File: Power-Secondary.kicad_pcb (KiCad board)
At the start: 2 copper layers, 82 x 66 mm, 37 parts, among them J1 SUPP PWR MON, J2 SUPP PWR 1, J3 SUPP PWR 2, J4 DCDC SUPPLY, J5 FUSE OUT, J6 SUPP OUT, J7 LV ENABLE, Q1 S1G1D2S2G2D1, Q1A1 IRFU5305PbF, Q1A2 IRFU5305PbF, Q1A3 IRFU5305PbF, Q1A4 IRFU5305PbF, Q2 S1G1D2S2G2D1, Q3 FDD86250-F085

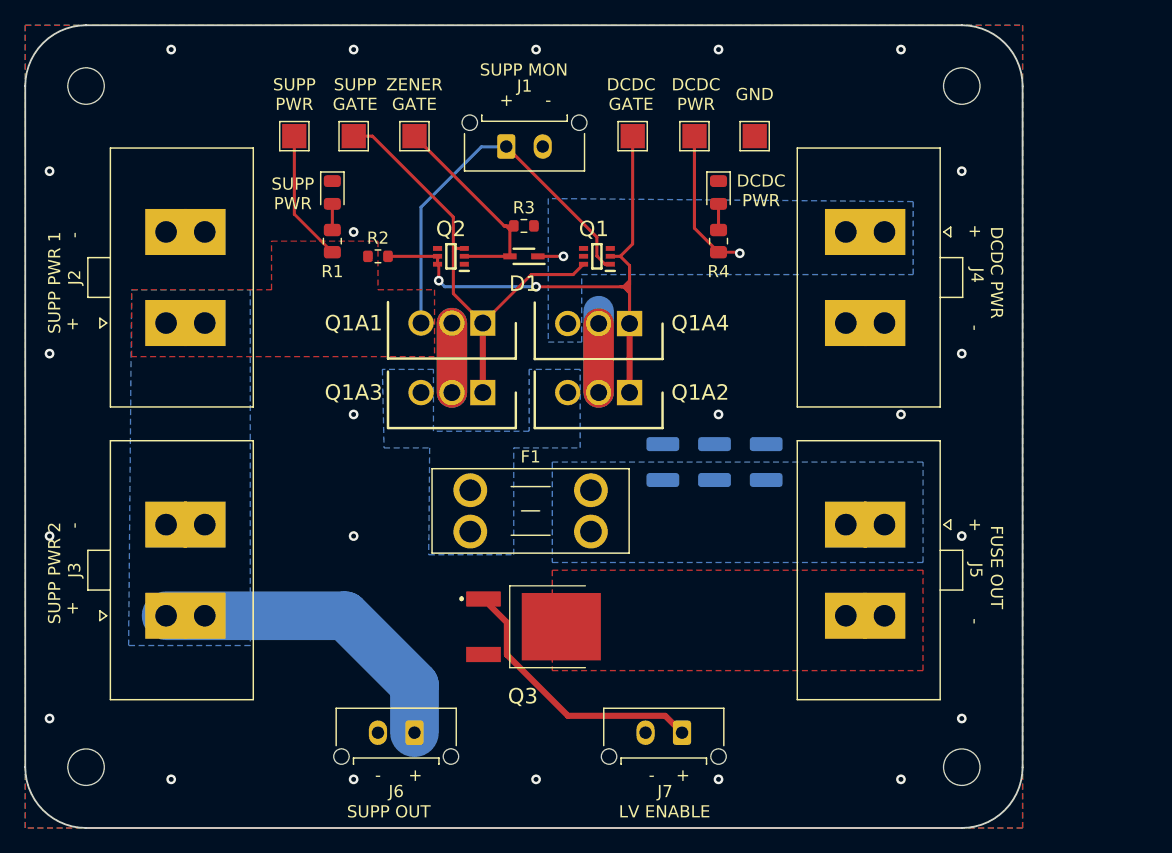
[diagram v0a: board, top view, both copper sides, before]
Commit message: Ltc4421 v1.0 (#12)
* LTC4421 Symbol creation

* early sch

* early sch

* changes

* Improved organization of sch

* added circuitry for sch

* Added MOSFET to symbol library

* Finished sch

* footprint assignments

* changes to Power Board sch

* CAD models, symbols update, and footprints

* Pull up and Pull down configs for VALID, DISABLE, SHDN, RETRY

* small changes

* Library fixes and sch changes

* Sch changes

* changes to sch

* assigned footprints

* Excel calculator

* Adjusted resistor divider values and specified more components in the BOM

* Completed BOM for the most part

* sch iteration 1 complete plssssssssss

* final footprint assignments

* initial layout

* added another current sense resistor

* fixed connector pinout

* change SHDN logic

* fixes to sch

* layout complete

* Layout fixes

* made all planes solid filled

* added supp mon connection

* constraint fixes

---------

Co-authored-by: choafe <cryn.hoang@gmail.com>
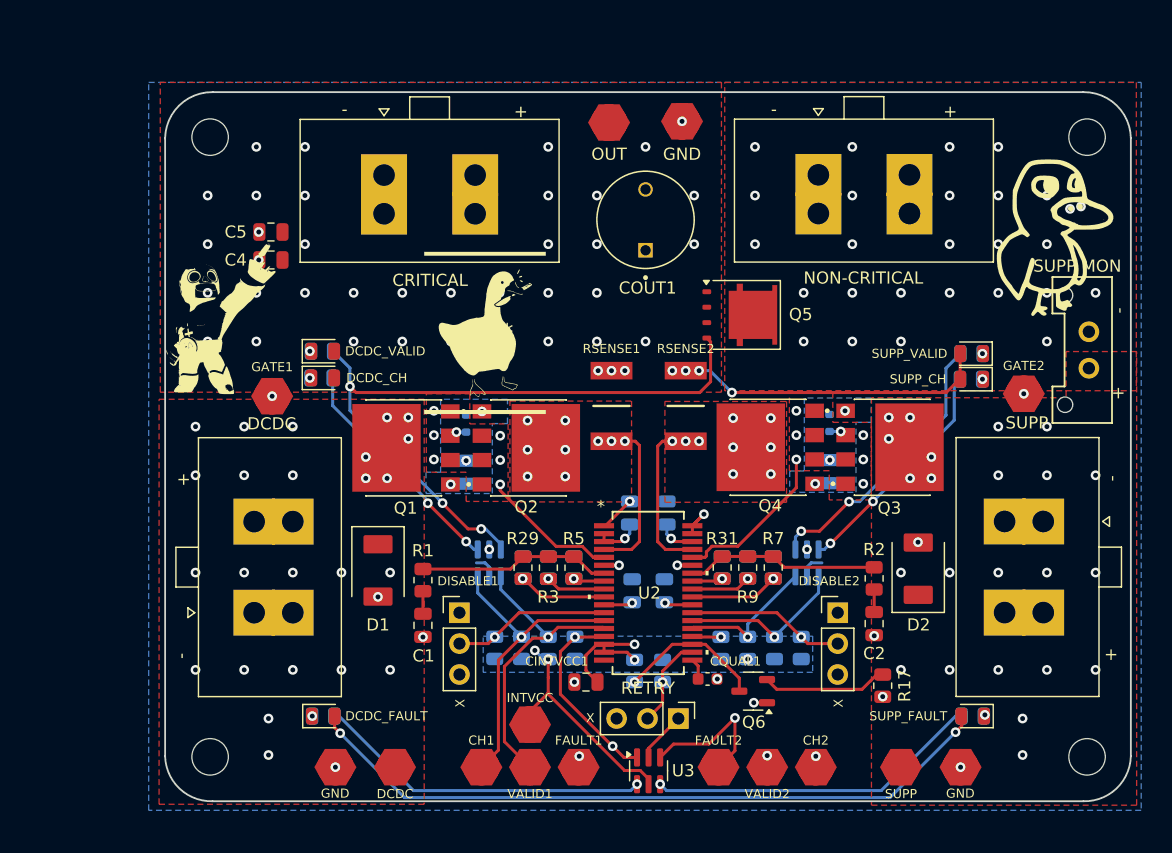
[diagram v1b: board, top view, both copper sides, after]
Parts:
- removed DS1: SUPP_PWR, Diode_SMD:D_0805_2012Metric
- removed DS2: DCDC_PWR, Diode_SMD:D_0805_2012Metric
- removed F1: Fuse, Fuse:Fuseholder_Blade_Mini_Keystone_3568
- removed J1: SUPP PWR MON, Connector_Molex:Molex_Micro-Fit_3.0_43650-0215_1x02_P3.00mm_Vertical
- removed J2: SUPP PWR 1, Connector_Molex:Molex_Sabre_43160-0102_1x02_P7.49mm_Vertical
- removed J3: SUPP PWR 2, Connector_Molex:Molex_Sabre_43160-0102_1x02_P7.49mm_Vertical
- removed J4: DCDC SUPPLY, Connector_Molex:Molex_Sabre_43160-0102_1x02_P7.49mm_Vertical
- removed J5: FUSE OUT, Connector_Molex:Molex_Sabre_43160-0102_1x02_P7.49mm_Vertical
- removed J6: SUPP OUT, Connector_Molex:Molex_Micro-Fit_3.0_43650-0215_1x02_P3.00mm_Vertical
- removed J7: LV ENABLE, Connector_Molex:Molex_Micro-Fit_3.0_43650-0215_1x02_P3.00mm_Vertical
- removed LOGO1: Dr Hallock, UTSVT_Special:Hallock_Image_Tiny
- removed LOGO2: UTSVT, UTSVT_Special:UTSVT_Logo_Symbol
- removed Q1A1, Q1A2, Q1A3, Q1A4: IRFU5305PbF, UTSVT_PowerSupp:SUP90P06-PCHAN-ENH-PWR-MOSFET
- removed TP1: SUPP_PWR, TestPoint:TestPoint_Pad_2.0x2.0mm
- removed TP2: DCDC_PWR, TestPoint:TestPoint_Pad_2.0x2.0mm
- removed TP3: ZENER_GATE, TestPoint:TestPoint_Pad_2.0x2.0mm
- removed TP4: DCDC_Gate, TestPoint:TestPoint_Pad_2.0x2.0mm
- removed TP5: Supp_Gate, TestPoint:TestPoint_Pad_2.0x2.0mm
- removed TP6: GND, TestPoint:TestPoint_Pad_2.0x2.0mm
- added ?: , , F.Cu at (113.5, 104.0)
- added ?: , , F.Cu at (164.9, 104.0)
- added C4: 10u, Capacitor_SMD:C_0805_2012Metric, F.Cu at (108.2, 62.3)
- added C5: 0.1u, Capacitor_SMD:C_0805_2012Metric, F.Cu at (108.2, 60.0)
- added CCPO1: 1u, Capacitor_SMD:C_0805_2012Metric, B.Cu at (137.7, 83.1)
- added CH1: TestPoint, UTSVT_Special:TestPoint_HEX_3mmID, F.Cu at (125.5, 104.0)
- added CH2: TestPoint, UTSVT_Special:TestPoint_HEX_3mmID, F.Cu at (153.0, 104.0)
- added CINTVCC1: 1u, Capacitor_SMD:C_0805_2012Metric, F.Cu at (134.1, 97.0)
- added CMOSFET1: 10u, Capacitor_SMD:C_0805_2012Metric, B.Cu at (124.2, 79.8)
- added CMOSFET3: 10u, Capacitor_SMD:C_0805_2012Metric, B.Cu at (154.2, 79.7)
- added COUT1: 1.2m, PowerBoardLib:EEUFS1C122LB, F.Cu at (139.0, 59.0)
- added CQUAL1: 500p, Capacitor_SMD:C_0603_1608Metric, F.Cu at (144.1, 96.8)
- added CRITICAL: PowerConn, Connector_Molex:Molex_Sabre_43160-0102_1x02_P7.49mm_Vertical, F.Cu at (117.5, 58.5)
- added CTMR1: 10u, Capacitor_SMD:C_0805_2012Metric, B.Cu at (137.9, 89.5)
- added CTMR2: 10u, Capacitor_SMD:C_0805_2012Metric, B.Cu at (140.6, 89.5)
- added D11: D_Zener, Diode_SMD:D_SOD-523, B.Cu at (154.1, 75.7)
- added D2: SMBJ15D-M3I, PowerBoardLib:P26_DO-214AA_SMB, F.Cu at (161.4, 89.8)
- added D9: D_Zener, Diode_SMD:D_SOD-523, B.Cu at (124.2, 75.8)
- added DCDC: TestPoint, UTSVT_Special:TestPoint_HEX_3mmID, F.Cu at (118.4, 104.0)
- added DCDC: PowerConn, Connector_Molex:Molex_Sabre_43160-0102_1x02_P7.49mm_Vertical, F.Cu at (110.0, 91.3)
- added DCDC_CH: LED, LED_SMD:LED_0805_2012Metric, F.Cu at (112.5, 72.0)
- added DCDC_FAULT: LED, LED_SMD:LED_0805_2012Metric, F.Cu at (112.5, 99.8)
- added DCDC_VALID: LED, LED_SMD:LED_0805_2012Metric, F.Cu at (112.5, 69.8)
- added DISABLE1: DIS1 Jumper, Connector_PinHeader_2.54mm:PinHeader_1x03_P2.54mm_Vertical, F.Cu at (123.7, 91.3)
- added DISABLE2: DIS2 Jumper, Connector_PinHeader_2.54mm:PinHeader_1x03_P2.54mm_Vertical, F.Cu at (154.8, 91.3)
- added FAULT1: TestPoint, UTSVT_Special:TestPoint_HEX_3mmID, F.Cu at (133.5, 104.0)
- added FAULT2: TestPoint, UTSVT_Special:TestPoint_HEX_3mmID, F.Cu at (145.0, 104.0)
- added G***: LOGO, LOGO, F.Cu at (103.8, 67.1)
- added G***: LOGO, LOGO, F.Cu at (125.8, 68.3)
- added G***: LOGO, LOGO, F.Cu at (172.6, 60.5)
- added G***: LOGO, LOGO, B.Cu at (112.8, 65.8)
- added G***: LOGO, LOGO, B.Cu at (166.2, 63.9)
- added G***: LOGO, LOGO, B.Cu at (139.1, 62.9)
- added GATE1: TestPoint, UTSVT_Special:TestPoint_HEX_3mmID, F.Cu at (108.3, 73.5)
- added GATE2: TestPoint, UTSVT_Special:TestPoint_HEX_3mmID, F.Cu at (170.1, 73.3)
- added GND: TestPoint, UTSVT_Special:TestPoint_HEX_3mmID, F.Cu at (142.0, 50.9)
- added INTVCC: TestPoint, UTSVT_Special:TestPoint_HEX_3mmID, F.Cu at (129.5, 100.5)
- added NON-CRITICAL: PowerConn, Connector_Molex:Molex_Sabre_43160-0102_1x02_P7.49mm_Vertical, F.Cu at (153.2, 58.5)
- added OUT: TestPoint, UTSVT_Special:TestPoint_HEX_3mmID, F.Cu at (136.0, 51.0)
- added Q4: SQJQ140E-T1_GE3, PowerBoardLib:TO200P800X182-5N, F.Cu at (149.2, 77.7)
- added Q5: SQJ141ELP, Package_SO:PowerPAK_SO-8L_Single, F.Cu at (146.8, 66.8)
- added Q6: PMOS, Package_TO_SOT_SMD:SOT-23-3, F.Cu at (147.8, 97.8)
- added R10: 261K, Resistor_SMD:R_0805_2012Metric, B.Cu at (147.4, 87.6)
- added R11: 100K, Resistor_SMD:R_0805_2012Metric, B.Cu at (112.5, 99.8)
- added R12: 100K, Resistor_SMD:R_0805_2012Metric, B.Cu at (165.9, 99.8)
- added R13: 100K, Resistor_SMD:R_0805_2012Metric, B.Cu at (165.8, 70.0)
- added R14: 100K, Resistor_SMD:R_0805_2012Metric, B.Cu at (165.8, 72.1)
- added R15: 100K, Resistor_SMD:R_0805_2012Metric, B.Cu at (112.4, 72.0)
- added R16: 100K, Resistor_SMD:R_0805_2012Metric, B.Cu at (112.4, 69.8)
- added R17: 100K, Resistor_SMD:R_0805_2012Metric, F.Cu at (158.5, 97.3)
- added R19: 100K, Resistor_SMD:R_0805_2012Metric, B.Cu at (126.6, 94.2)
- added R20: 100K, Resistor_SMD:R_0805_2012Metric, B.Cu at (151.8, 94.2)
- added R21: 100K, Resistor_SMD:R_0805_2012Metric, B.Cu at (128.8, 94.2)
- added R22: 100K, Resistor_SMD:R_0805_2012Metric, B.Cu at (149.6, 94.2)
- added R23: 100K, Resistor_SMD:R_0805_2012Metric, B.Cu at (131.0, 94.2)
- added R24: 100K, Resistor_SMD:R_0805_2012Metric, B.Cu at (147.4, 94.2)
- added R25: 100K, Resistor_SMD:R_0805_2012Metric, B.Cu at (133.2, 94.2)
- added R26: 100K, Resistor_SMD:R_0805_2012Metric, B.Cu at (145.2, 94.2)
- added R27: 100K, Resistor_SMD:R_0805_2012Metric, B.Cu at (140.4, 96.1)
- added R28: 100K, Resistor_SMD:R_0805_2012Metric, B.Cu at (138.1, 96.1)
- added R29: 5.76M, Resistor_SMD:R_0805_2012Metric, F.Cu at (128.9, 87.6)
- added R30: 215K, Resistor_SMD:R_0805_2012Metric, B.Cu at (128.9, 87.6)
- added R31: 5.76M, Resistor_SMD:R_0805_2012Metric, F.Cu at (145.3, 87.6)
- added R32: 287K, Resistor_SMD:R_0805_2012Metric, B.Cu at (145.3, 87.6)
- added R5: 5.76M, Resistor_SMD:R_0805_2012Metric, F.Cu at (133.1, 87.6)
- added R6: 287K, Resistor_SMD:R_0805_2012Metric, B.Cu at (133.1, 87.6)
- added R7: 5.76M, Resistor_SMD:R_0805_2012Metric, F.Cu at (149.5, 87.6)
- added R8: 215K, Resistor_SMD:R_0805_2012Metric, B.Cu at (149.5, 87.6)
- added R9: 5.76M, Resistor_SMD:R_0805_2012Metric, F.Cu at (147.4, 87.6)
- added RETRY: RETRY Jumper, Connector_PinHeader_2.54mm:PinHeader_1x03_P2.54mm_Vertical, F.Cu at (141.7, 100.0)
- added RSENSE1: 1m, PowerBoardLib:RESC6432X89N, F.Cu at (136.2, 74.3)
- added RSENSE2: 1m, PowerBoardLib:RESC6432X89N, F.Cu at (142.3, 74.3)
- added SUPP: PowerConn, Connector_Molex:Molex_Sabre_43160-0102_1x02_P7.49mm_Vertical, F.Cu at (168.5, 83.8)
- added SUPP MON: PowerConn, UTSVT_Connectors:Molex_MicroFit3.0_1x2xP3.00mm_PolarizingPeg_Vertical, F.Cu at (175.4, 71.2)
- added SUPP: TestPoint, UTSVT_Special:TestPoint_HEX_3mmID, F.Cu at (160.0, 104.0)
- added SUPP_CH: LED, LED_SMD:LED_0805_2012Metric, F.Cu at (165.8, 72.1)
- added SUPP_FAULT: LED, LED_SMD:LED_0805_2012Metric, F.Cu at (165.9, 99.8)
- added SUPP_VALID: LED, LED_SMD:LED_0805_2012Metric, F.Cu at (165.8, 70.0)
- added U2: LTC4421CG-PBF, PowerBoardLib:G_05-08-1640_ADI, F.Cu at (139.2, 89.7)
- added U3: 74LVC2G07GV,125, Package_TO_SOT_SMD:ROHM_SOT-457_ClockwisePinNumbering, F.Cu at (139.2, 104.3)
- added U4: 74LVC2G07GV,125, Package_TO_SOT_SMD:ROHM_SOT-457_ClockwisePinNumbering, B.Cu at (152.3, 87.2)
- added U5: 74LVC2G07GV,125, Package_TO_SOT_SMD:ROHM_SOT-457_ClockwisePinNumbering, B.Cu at (126.2, 87.2)
- added VALID1: TestPoint, UTSVT_Special:TestPoint_HEX_3mmID, F.Cu at (129.5, 104.0)
- added VALID2: TestPoint, UTSVT_Special:TestPoint_HEX_3mmID, F.Cu at (149.0, 104.0)
- C1, C2: value 100uF -> 10u; footprint Capacitor_SMD:C_1210_3225Metric -> Capacitor_SMD:C_0805_2012Metric; moved to F.Cu
- C3: value 100uF -> 0.1u; footprint Capacitor_SMD:C_1210_3225Metric -> Capacitor_SMD:C_0805_2012Metric
- D1: value 10V -> SMBJ15D-M3I; footprint UTSVT_PowerSupp:SOD2512X110N -> PowerBoardLib:P26_DO-214AA_SMB
- H1, H2, H3, H4: value M3 -> MountingHole
- Q1, Q2: value S1G1D2S2G2D1 -> SQJQ140E-T1_GE3; footprint UTSVT_PowerSupp:SOT65P210X100-6N -> PowerBoardLib:TO200P800X182-5N
- Q3: value FDD86250-F085 -> SQJQ140E-T1_GE3; footprint UTSVT_PowerSupp:FDD13AN06A0F085 -> PowerBoardLib:TO200P800X182-5N
- R1: value 5.1K -> 1.2
- R2: value 10k -> 1.2; footprint Resistor_SMD:R_0603_1608Metric -> Resistor_SMD:R_0805_2012Metric
- R3: value 1M -> 5.76M; footprint Resistor_SMD:R_0603_1608Metric -> Resistor_SMD:R_0805_2012Metric
- R4: value 5.1K -> 261K; moved to B.Cu
- moved H4 82.3 mm to (175.3, 103.1)
- moved H3 61.8 mm to (103.2, 103.1)
- moved R2 48.6 mm to (157.8, 88.5), turned to -90 degrees
- moved C1 31.3 mm to (120.7, 92.3), turned to -90 degrees
- moved Q3 30.8 mm to (159.1, 77.7), turned to 0 degrees
- moved R4 30.3 mm to (131.0, 87.6)
- moved R1 28.9 mm to (120.7, 88.6), turned to -90 degrees
- moved R3 28.2 mm to (131.0, 87.6), turned to -90 degrees
- moved D1 26.5 mm to (117.0, 85.7), turned to -90 degrees
- moved Q1 22.2 mm to (119.3, 77.8)
- moved C2 18.7 mm to (157.8, 92.2), turned to -90 degrees
- moved Q2 16.9 mm to (129.2, 77.8), turned to 0 degrees
- moved H2 11.1 mm to (175.3, 52.2)
- moved H1 11.0 mm to (103.2, 52.2)
- moved C3 4.20 mm to (140.8, 83.1)
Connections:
- C1 pad 1: FUSE_OUT -> Net-(C1-Pad1)
- C1 pad 2: GNDS -> GND
- C2 pad 1: FUSE_OUT -> Net-(C2-Pad1)
- C2 pad 2: GNDS -> GND
- C3 pad 1: FUSE_OUT -> /OUT
- C3 pad 2: GNDS -> GND
- D1 pad 1: DCDC_PWR -> /V1
- D1 pad 2: ZENER_GATE -> GND
- Q1 pad 1: SUPP_PWR -> /GATE1
- Q1 pad 2: DCDC_Gate -> /SOURCE1
- Q1 pad 3: (no net) -> /SOURCE1
- Q1 pad 4: (no net) -> /SOURCE1
- Q1 pad 5: (no net) -> /V1
- Q2 pad 1: GNDS -> /GATE1
- Q2 pad 2: ZENER_GATE -> /SOURCE1
- Q2 pad 3: Supp_Gate -> /SOURCE1
- Q2 pad 4: GNDS -> /SOURCE1
- Q2 pad 5: DCDC_Gate -> /LTC4421/SENSE1
- Q3 pad 1: Net-(J7-Pin_1) -> /GATE2
- Q3 pad 2: Net-(J5-Pin_2) -> /SOURCE2
- Q3 pad 3: GNDS -> /SOURCE2
- R1 pad 1: SUPP_PWR -> /V1
- R1 pad 2: Net-(DS1-A) -> Net-(C1-Pad1)
- R2 pad 1: SUPP_PWR -> /V2
- R2 pad 2: DCDC_Gate -> Net-(C2-Pad1)
- R3 pad 1: ZENER_GATE -> /V1
- R3 pad 2: GNDS -> /LTC4421/UVR1
- R4 pad 1: DCDC_PWR -> /LTC4421/UVR1
- R4 pad 2: Net-(DS2-A) -> GND
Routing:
- net /V2: track 0.00 -> 84.0 mm, vias 0 -> 25
- net SUPP_PWR: track 69.6 -> 0.00 mm
- net /OUT: track 0.00 -> 64.2 mm, vias 0 -> 42
- net /LTC4421/Non-Crit Drive: track 0.00 -> 56.8 mm, vias 0 -> 3
- net /INTVCC: track 0.00 -> 50.8 mm, vias 0 -> 7
- net DCDC_Gate: track 47.4 -> 0.00 mm, vias 2 -> 0
- net Supp_Gate: track 38.1 -> 0.00 mm
- net /GATE1: track 0.00 -> 35.7 mm, vias 0 -> 4
- net /GATE2: track 0.00 -> 30.9 mm, vias 0 -> 4
- net Net-(U3-1Y): track 0.00 -> 27.6 mm, vias 0 -> 1
- net Net-(U3-2Y): track 0.00 -> 27.5 mm, vias 0 -> 1
- net /LTC4421/CH1: track 0.00 -> 25.9 mm, vias 0 -> 1
- net /LTC4421/CH2: track 0.00 -> 25.7 mm, vias 0 -> 2
- net /LTC4421/VALID1: track 0.00 -> 25.3 mm, vias 0 -> 1
- net Net-(U4-1Y): track 0.00 -> 23.1 mm, vias 0 -> 2
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- added copper zone on B.Cu, net /GATE1
- added copper zone on B.Cu, net /GATE2
- added copper zone on B.Cu, net /INTVCC
- added copper zone on F.Cu, net /LTC4421/SENSE1
- added copper zone on In1.Cu, net /LTC4421/SENSE1
- added copper zone on In2.Cu, net /LTC4421/SENSE1
- added copper zone on F.Cu, net /LTC4421/SENSE2
- added copper zone on In1.Cu, net /LTC4421/SENSE2
- added copper zone on In2.Cu, net /LTC4421/SENSE2
- added copper zone on F.Cu, net /OUT
- added copper zone on In1.Cu, net /OUT
- added copper zone on In2.Cu, net /OUT
- added copper zone on F.Cu, net /SOURCE1
- added copper zone on In1.Cu, net /SOURCE1
- added copper zone on In2.Cu, net /SOURCE1
- added copper zone on F.Cu, net /SOURCE2
- added copper zone on In1.Cu, net /SOURCE2
- added copper zone on In2.Cu, net /SOURCE2
- added copper zone on F.Cu, net /V1
- added copper zone on In1.Cu, net /V1
- added copper zone on In2.Cu, net /V1
- added copper zone on F.Cu, net /V2
- added copper zone on In1.Cu, net /V2
- added copper zone on In2.Cu, net /V2
- added copper zone on B.Cu, net GND
- added copper zone on F.Cu, net Net-(J4-Pin_2)
- added copper zone on In1.Cu, net Net-(J4-Pin_2)
- added copper zone on In2.Cu, net Net-(J4-Pin_2)
- removed copper zone on B.Cu, net DCDC_PWR
- removed copper zone on B.Cu, net FUSE_OUT
- removed copper zone on B.Cu, net GNDS
- removed copper zone on F.Cu, net GNDS
- removed copper zone on B.Cu, net Net-(F1-Pad1)
- removed copper zone on F.Cu, net Net-(J5-Pin_2)
- removed copper zone on B.Cu, net SUPP_PWR
- removed copper zone on F.Cu, net SUPP_PWR
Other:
- board size 82 x 66 mm -> 79.4 x 58.3 mm
- copper layers 2 -> 4
- board text added: "Designed by: Frank Li & Carolyn Hoang"
- board text added: "X"
- board text removed: "DCDC GATE"
- board text removed: "DCDC PWR"
- board text removed: "FUSE OUT"
- board text removed: "Jason and Pratyush"
- board text removed: "LV ENABLE"
- board text removed: "SUPP GATE"
- board text removed: "SUPP MON"
- board text removed: "SUPP OUT"
- board text removed: "SUPP PWR"
- board text removed: "SUPP PWR 1"
- board text removed: "SUPP PWR 2"
- board text removed: "ZENER GATE"
- board text removed: "{dblquote}Rabid{dblquote}, not rabbit."

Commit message: fixes for IGN and non-crit
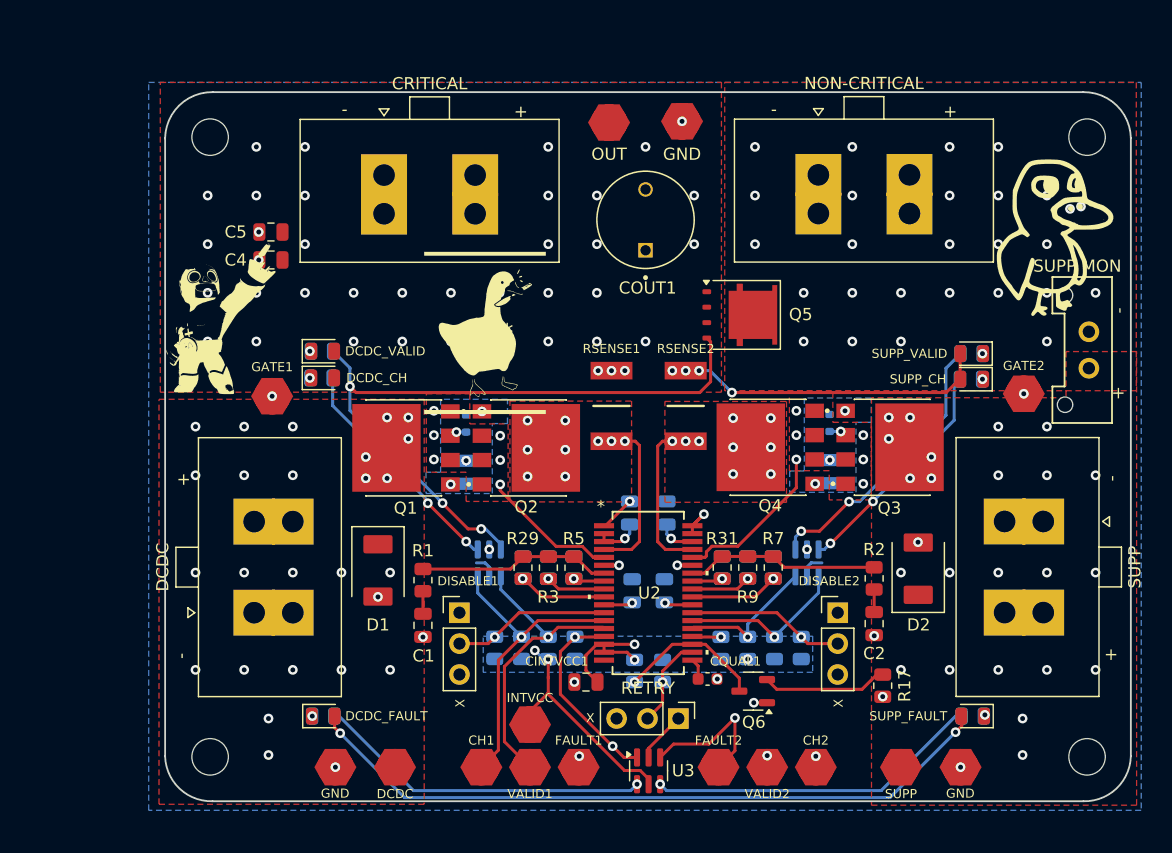
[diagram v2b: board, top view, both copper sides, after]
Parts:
- CRITICAL, DCDC, NON-CRITICAL, SUPP: footprint Connector_Molex:Molex_Sabre_43160-0102_1x02_P7.49mm_Vertical -> Library:Molex_Sabre_43160-0102_1x02_P7.49mm_Vertical
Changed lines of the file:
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@@
 		)
 	)
-	(footprint "Connector_Molex:Molex_Sabre_43160-0102_1x02_P7.49mm_Vertical"
+	(footprint "Library:Molex_Sabre_43160-0102_1x02_P7.49mm_Vertical"
 		(layer "F.Cu")
 		(at 168.52 83.8 -90)
@@
 		(tags "connector Molex Sabre side entry")
 		(property "Reference" "SUPP"
-			(at -8.11 -1.83 180)
+			(at 3.75 -10.7 -90)
 			(layer "F.SilkS")
 			(effects
@@
 		)
 		(property "Value" "PowerConn"
-			(at 3.75 5.08 90)
+			(at 3.75 5.08 -90)
 			(layer "F.Fab")
 			(effects
@@
 			)
 		)
-		(property ki_fp_filters "Connector*:*_1x??_*")
-		(sheetname "Root")
-		(sheetfile "Power-Secondary.kicad_sch")
 		(attr through_hole)
 		(fp_line
@@
 		)
 		(fp_text user "${REFERENCE}"
-			(at 3.75 3.18 90)
+			(at 3.75 3.18 -90)
 			(layer "F.Fab")
 			(effects
@@
 			(pintype "passive")
 		)
-		(model "${KICAD8_3DMODEL_DIR}/Connector_Molex.3dshapes/Molex_Sabre_43160-0102_1x02_P7.49mm_Vertical.wrl"
+		(model "${KIPRJMOD}/UTSVT-KiCadLibraries/utsvt3d/connectors.3dshapes/431600102.stp"
 			(offset
-				(xyz 0 0 0)
+				(xyz 4 2 7.5)
 			)
 			(scale
@@
 			)
 			(rotate
-				(xyz 0 0 0)
+				(xyz -90 0 -180)
 			)
 		)
@@
 		)
 	)
-	(footprint "Connector_Molex:Molex_Sabre_43160-0102_1x02_P7.49mm_Vertical"
+	(footprint "Library:Molex_Sabre_43160-0102_1x02_P7.49mm_Vertical"
 		(layer "F.Cu")
 		(at 153.21 58.48)
@@
 		(tags "connector Molex Sabre side entry")
 		(property "Reference" "NON-CRITICAL"
-			(at 3.7 5.3 0)
+			(at 3.75 -10.7 0)
 			(layer "F.SilkS")
 			(effects
@@
 			)
 		)
-		(property ki_fp_filters "Connector*:*_1x??_*")
-		(sheetname "Root")
-		(sheetfile "Power-Secondary.kicad_sch")
 		(attr through_hole)
 		(fp_line
@@
 			(pintype "passive")
 		)
-		(model "${KICAD8_3DMODEL_DIR}/Connector_Molex.3dshapes/Molex_Sabre_43160-0102_1x02_P7.49mm_Vertical.wrl"
+		(model "${KIPRJMOD}/UTSVT-KiCadLibraries/utsvt3d/connectors.3dshapes/431600102.stp"
 			(offset
-				(xyz 0 0 0)
+				(xyz 4 2 7.5)
 			)
 			(scale
@@
 			)
 			(rotate
-				(xyz 0 0 0)
+				(xyz -90 0 -180)
 			)
 		)
@@
 		)
 	)
-	(footprint "Connector_Molex:Molex_Sabre_43160-0102_1x02_P7.49mm_Vertical"
+	(footprint "Library:Molex_Sabre_43160-0102_1x02_P7.49mm_Vertical"
 		(layer "F.Cu")
 		(at 117.5 58.5)
@@
 		(tags "connector Molex Sabre side entry")
 		(property "Reference" "CRITICAL"
-			(at 3.79 5.47 0)
+			(at 3.75 -10.7 0)
 			(layer "F.SilkS")
 			(effects
@@
 			)
 		)
-		(property ki_fp_filters "Connector*:*_1x??_*")
-		(sheetname "Root")
-		(sheetfile "Power-Secondary.kicad_sch")
 		(attr through_hole)
 		(fp_line
@@
 			(pintype "passive")
 		)
-		(model "${KICAD8_3DMODEL_DIR}/Connector_Molex.3dshapes/Molex_Sabre_43160-0102_1x02_P7.49mm_Vertical.wrl"
+		(model "${KIPRJMOD}/UTSVT-KiCadLibraries/utsvt3d/connectors.3dshapes/431600102.stp"
 			(offset
-				(xyz 0 0 0)
+				(xyz 4 2 7.5)
 			)
 			(scale
@@
 			)
 			(rotate
-				(xyz 0 0 0)
+				(xyz -90 0 -180)
 			)
 		)
@@
 		)
 	)
-	(footprint "Connector_Molex:Molex_Sabre_43160-0102_1x02_P7.49mm_Vertical"
+	(footprint "Library:Molex_Sabre_43160-0102_1x02_P7.49mm_Vertical"
 		(layer "F.Cu")
 		(at 110 91.3 90)
@@
 		(tags "connector Molex Sabre side entry")
 		(property "Reference" "DCDC"
-			(at 15.535 -1.74 0)
+			(at 3.75 -10.7 90)
 			(layer "F.SilkS")
 			(effects
@@
 		)
 		(property "Value" "PowerConn"
-			(at 3.75 5.08 -90)
+			(at 3.75 5.08 90)
 			(layer "F.Fab")
 			(effects
@@
 			)
 		)
-		(property ki_fp_filters "Connector*:*_1x??_*")
-		(sheetname "Root")
-		(sheetfile "Power-Secondary.kicad_sch")
 		(attr through_hole)
 		(fp_line
@@
 		)
 		(fp_text user "${REFERENCE}"
-			(at 3.75 3.18 -90)
+			(at 3.75 3.18 90)
 			(layer "F.Fab")
 			(effects
@@
 			(pintype "passive")
 		)
-		(model "${KICAD8_3DMODEL_DIR}/Connector_Molex.3dshapes/Molex_Sabre_43160-0102_1x02_P7.49mm_Vertical.wrl"
+		(model "${KIPRJMOD}/UTSVT-KiCadLibraries/utsvt3d/connectors.3dshapes/431600102.stp"
 			(offset
-				(xyz 0 0 0)
+				(xyz 4 2 7.5)
 			)
 			(scale
@@
 			)
 			(rotate
-				(xyz 0 0 0)
+				(xyz -90 0 -180)
 			)
 		)

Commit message: SHDN, non-crit, and ignition sequence fixes
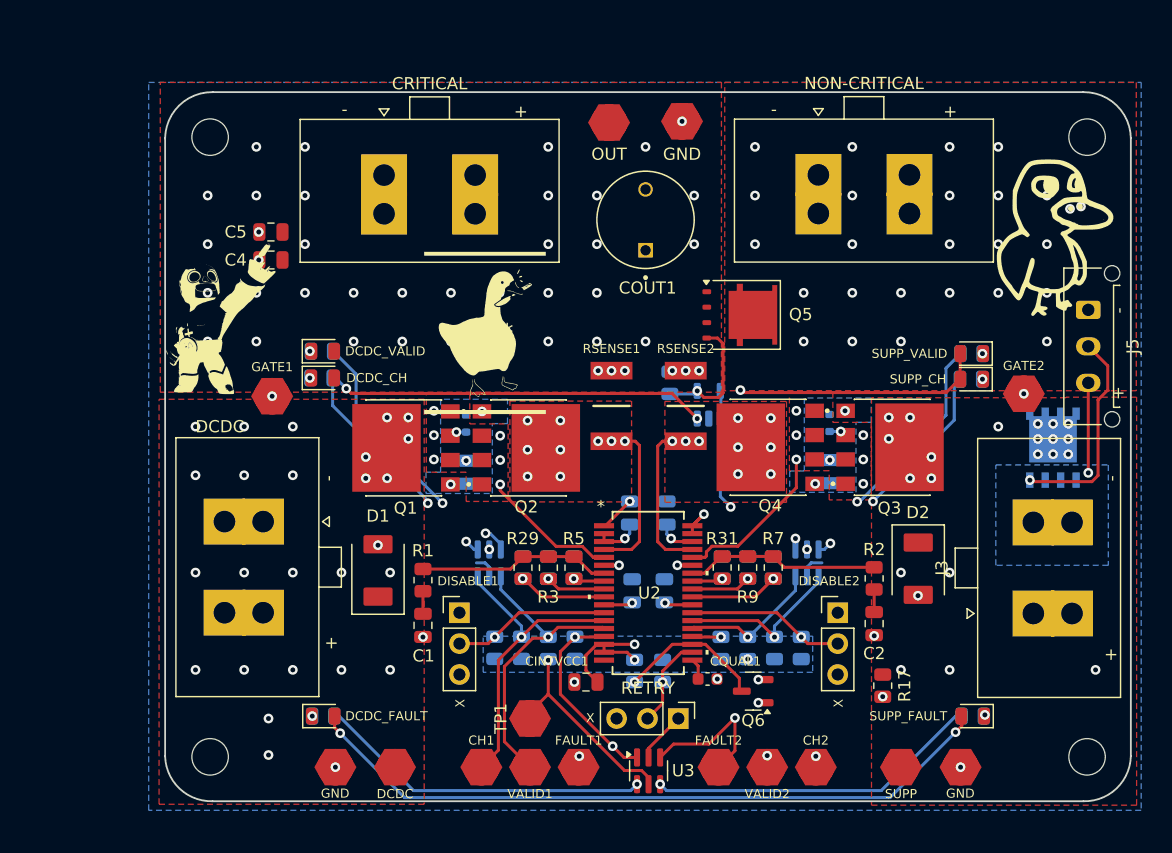
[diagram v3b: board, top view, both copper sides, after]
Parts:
- removed INTVCC: TestPoint, UTSVT_Special:TestPoint_HEX_3mmID
- removed the SUPP at (168.5, 83.8)
- removed SUPP MON: PowerConn, UTSVT_Connectors:Molex_MicroFit3.0_1x2xP3.00mm_PolarizingPeg_Vertical
- added J3: PowerConn, Connector_Molex:Molex_Sabre_43160-0102_1x02_P7.49mm_Vertical, F.Cu at (174.1, 91.4)
- added J5: Conn_01x03, Connector_Molex:Molex_Micro-Fit_3.0_43650-0315_1x03_P3.00mm_Vertical, F.Cu at (175.4, 66.4)
- added Q7: PMOS, Package_SO:PowerPAK_SO-8_Single, B.Cu at (172.5, 77.7)
- added R18: 10K, Resistor_SMD:R_0805_2012Metric, B.Cu at (141.0, 72.4)
- added TP1: TestPoint, UTSVT_Special:TestPoint_HEX_3mmID, F.Cu at (129.5, 100.0)
- added U1: LM397, Package_TO_SOT_SMD:SOT-23-5, B.Cu at (144.2, 74.2)
- Q6: value PMOS -> NMOS; footprint Package_TO_SOT_SMD:SOT-23-3 -> Package_TO_SOT_SMD:SOT-23
- R30, R8: value 215K -> 226K
- R31, R5: value 5.76M -> 5.69M
- R32, R6: value 287K -> 277K
- moved DCDC 9.36 mm to (104.4, 83.8), turned to -90 degrees
- moved D1 4.30 mm to (117.0, 90.0), turned to 90 degrees
- moved D2 4.30 mm to (161.4, 85.5), turned to -90 degrees
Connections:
- net /INTVCC renamed /LTC4421/INTVCC
- Q5 pad 4: /LTC4421/Non-Crit Drive -> Net-(Q5-Pad4)
- Q6 pad 1: GND -> /SHDN
- Q6 pad 2: /V2 -> /SHDN_sig
- Q6 pad 3: /SHDN -> GND
- R13 pad 2: Net-(U4-1Y) -> /SHDN_sig
- R15 pad 2: Net-(U5-1Y) -> /LTC4421/Non-Crit Drive
- R16 pad 2: /LTC4421/Non-Crit Drive -> Net-(U5-2Y)
- U4 pad 6: Net-(U4-1Y) -> /SHDN_sig
- U5 pad 4: /LTC4421/Non-Crit Drive -> Net-(U5-2Y)
- U5 pad 6: Net-(U5-1Y) -> /LTC4421/Non-Crit Drive
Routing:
- net /SHDN_sig: track 0.00 -> 37.8 mm, vias 0 -> 3
- net Net-(U4-1Y): track 23.1 -> 0.00 mm, vias 2 -> 0
- net Net-(U5-2Y): track 0.00 -> 22.9 mm, vias 0 -> 2
- net Net-(U5-1Y): track 19.2 -> 0.00 mm, vias 2 -> 0
- net Net-(J5-Pin_2): track 0.00 -> 17.5 mm, vias 0 -> 1
- net /LTC4421/INTVCC: track 50.8 -> 67.8 mm
- net Net-(Q5-Pad4): track 0.00 -> 10.5 mm, vias 0 -> 1
- net /V2: track 84.0 -> 74.0 mm, vias 25 -> 23
- net Net-(J3-Pin_2): track 0.00 -> 7.40 mm, vias 0 -> 1
- net /LTC4421/Non-Crit Drive: track 56.8 -> 50.6 mm, vias 3 -> 4
- net /OUT: track 64.2 -> 63.1 mm
- net Net-(J4-Pin_2): vias 27 -> 26
- added copper zone on B.Cu, net Net-(J3-Pin_2)
